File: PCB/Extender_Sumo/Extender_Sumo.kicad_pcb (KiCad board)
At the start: 2 copper layers, 60 x 46 mm, 35 parts, among them J1 CNY70 FR, J10 CNY70 BL, J11 Left Encoder, J12 Extra Pins, J13 Conn_02x14_Odd_Even, J14 IR Module, J15 Bluetooth, J16 Optocoupler Out, J17 MPU6050 I2C, J18 Conn_01x03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

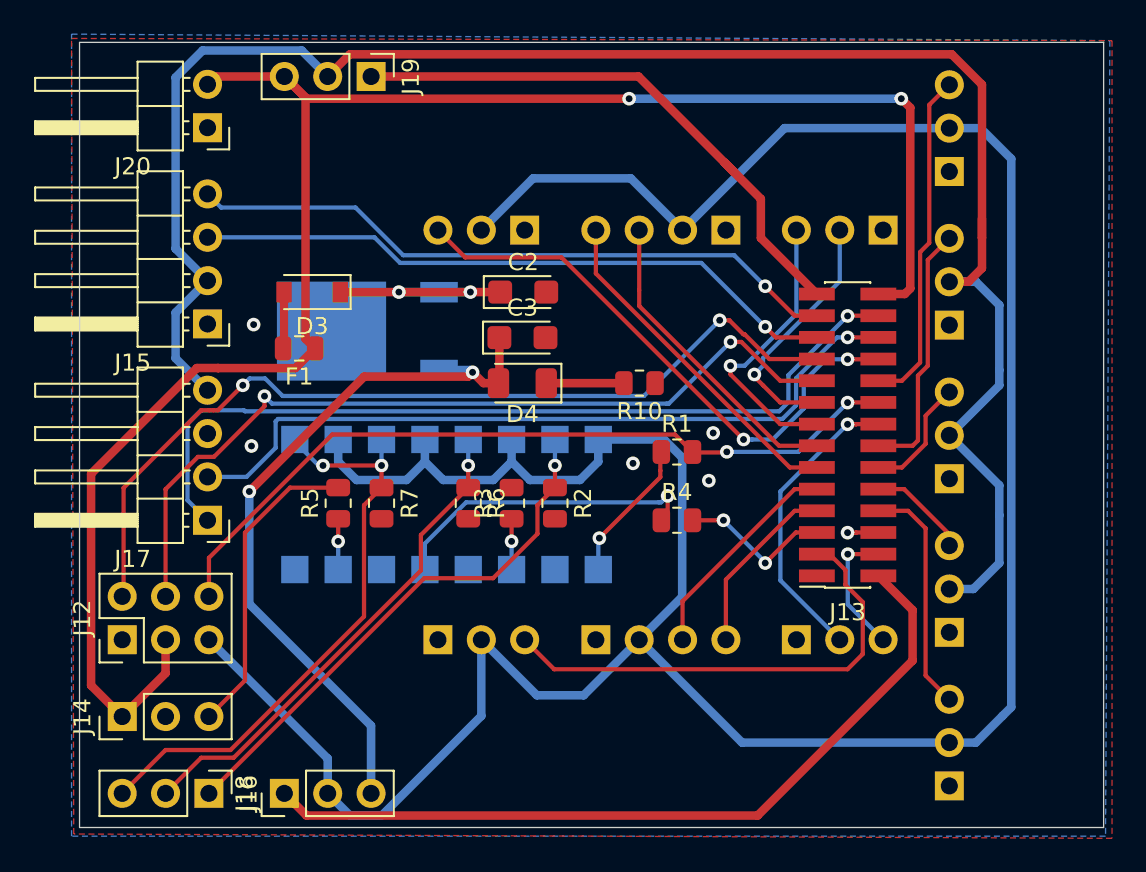
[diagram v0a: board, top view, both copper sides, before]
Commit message: Added mounting holes
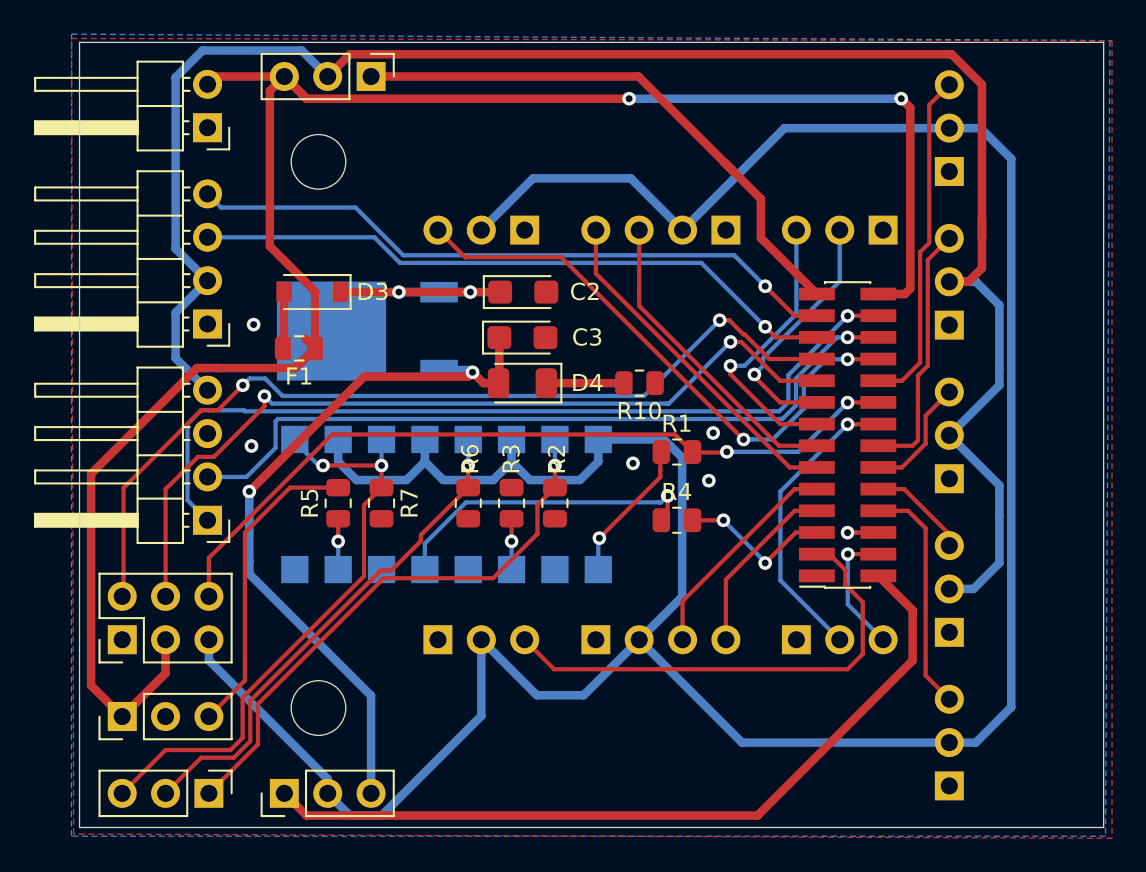
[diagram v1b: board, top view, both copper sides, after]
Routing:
- net VPP: track 108.5 -> 111.7 mm
- net Net-(J16-Pad1): track 31.5 -> 32.9 mm
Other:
- outline, holes or cut-outs redrawn

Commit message: WS1812B Working Update
Added WS2812B libraries.
Added WS2812B pin to CubeMX.
Fixed PCB errors with WS2812B.
TODO:
Replace LTV-356 with faster chip
MIC5205 needs to be replaced for higher power
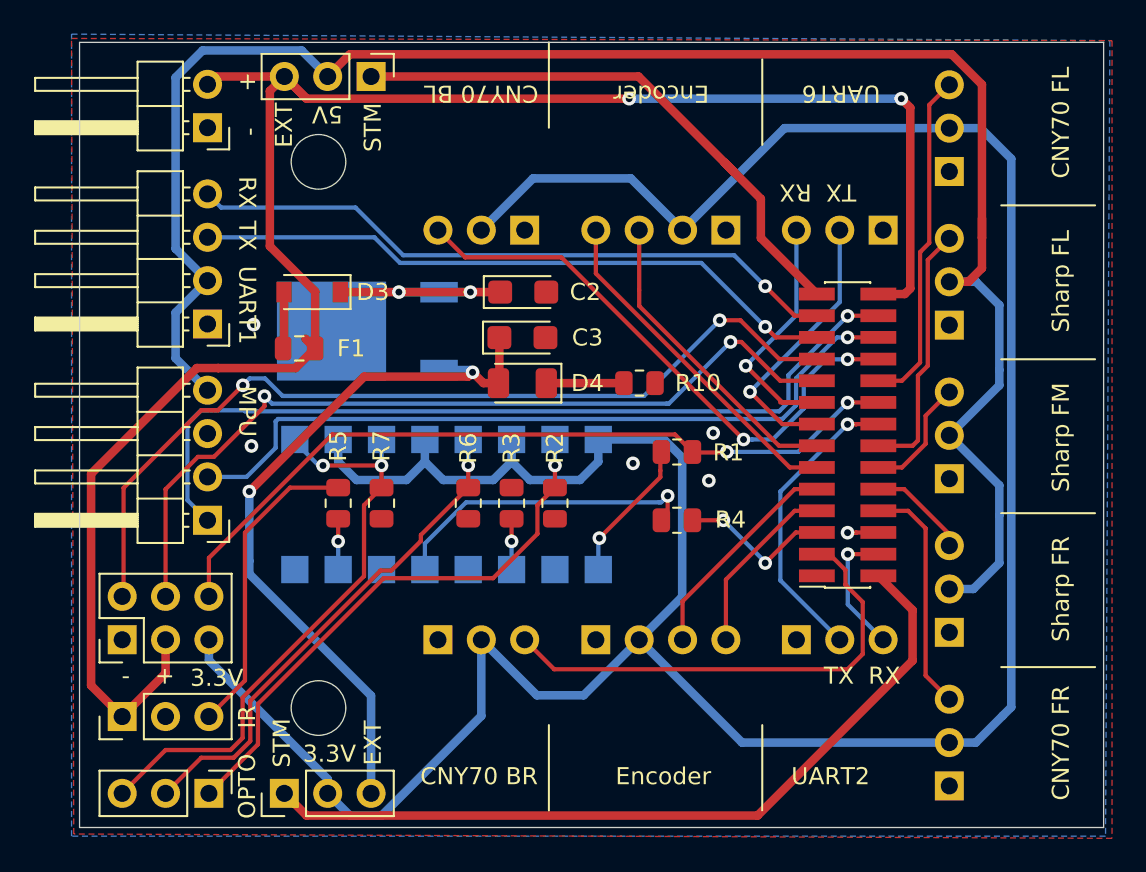
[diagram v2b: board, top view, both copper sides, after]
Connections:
- J7 pad 2: PC7 -> PC6
- J7 pad 3: PC6 -> PC7
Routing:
- net PC7: track 15.7 -> 17.1 mm
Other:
- board text added: "+"
- board text added: "-"
- board text added: "3.3V"
- board text added: "5V"
- board text added: "CNY70 BL"
- board text added: "CNY70 BR"
- board text added: "CNY70 FL"
- board text added: "CNY70 FR"
- board text added: "EXT"
- board text added: "Encoder"
- board text added: "IR"
- board text added: "MPU"
- board text added: "OPTO"
- board text added: "RX"
- board text added: "STM"
- board text added: "Sharp FL"
- board text added: "Sharp FM"
- board text added: "Sharp FR"
- board text added: "TX"
- board text added: "UART1"
- board text added: "UART2"
- board text added: "UART6"
